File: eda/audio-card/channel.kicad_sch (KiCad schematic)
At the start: 2 parts, among them U3 74HCT541, U4 74HCT541

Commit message: Interim commit
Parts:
- removed U3, U4: 74HCT541, Package_DIP:DIP-20_W7.62mm, symbol 74xx:74HCT541
- added U1: 74LS74, symbol 74ls593:74LS74
- added U2, U5: 74LS593, Package_DIP:DIP-20_W7.62mm, symbol counters:74LS593
- added U4, U6: 74HCT574, Package_DIP:DIP-20_W7.62mm, symbol 74ls593:74HCT574
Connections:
- net D0: now also U5.1 (A), U6.2 (D0)
- net D1: now also U5.2 (B), U6.3 (D1)
- net D2: now also U5.3 (C), U6.4 (D2)
- net D3: now also U5.4 (D), U6.5 (D3)
- net D4: now also U5.5 (E), U6.6 (D4)
- net D5: now also U5.7 (G), U6.7 (D5)
- net D6: now also U5.7 (G), U6.8 (D6)
- net D7: now also U5.8 (H), U6.9 (D7)
- net GND: now also U2.10 (GND), U2.14 (~{CCKEN}), U4.10 (GND), U5.10 (GND), U6.1 (OE), U6.10 (GND)
- net VCC: now also U2.16 (RCK), U2.20 (VCC), U4.20 (VCC), U5.13 (CCK), U5.15 (CCKEN), U5.16 (RCK), U5.20 (VCC), U6.20 (VCC)
- new net: U2.1 (A), U6.19 (Q0)
- new net: U2.11 (~{RCO}), U5.14 (~{CCKEN})
- new net: U2.2 (B), U6.18 (Q1)
- new net: U2.3 (C), U6.17 (Q2)
- new net: U2.4 (D), U6.16 (Q3)
- new net: U2.5 (E), U6.15 (Q4)
- new net: U2.7 (G), U6.13 (Q6)
- new net: U2.7 (G), U6.14 (Q5)
- new net: U2.8 (H), U6.12 (Q7)
- new net: U1.3 (C), U5.11 (~{RCO})
- new net: U1.2 (D), U1.6 (~{Q})
- new net MainClock: U2.13 (CCK)
- new net Tone: U1.5 (Q), U4.1 (OE)
- new net ~{NoteLatch}: U2.17 (~{RCKEN}), U5.17 (~{RCKEN})
- new net ~{OctaveLatch}: U6.11 (Cp)
- new net ~{Reset}: U2.12 (~{CCLR}), U2.9 (~{CLOAD}), U5.12 (~{CCLR}), U5.9 (~{CLOAD})
- new net ~{VolumeLatch}: U4.11 (Cp)

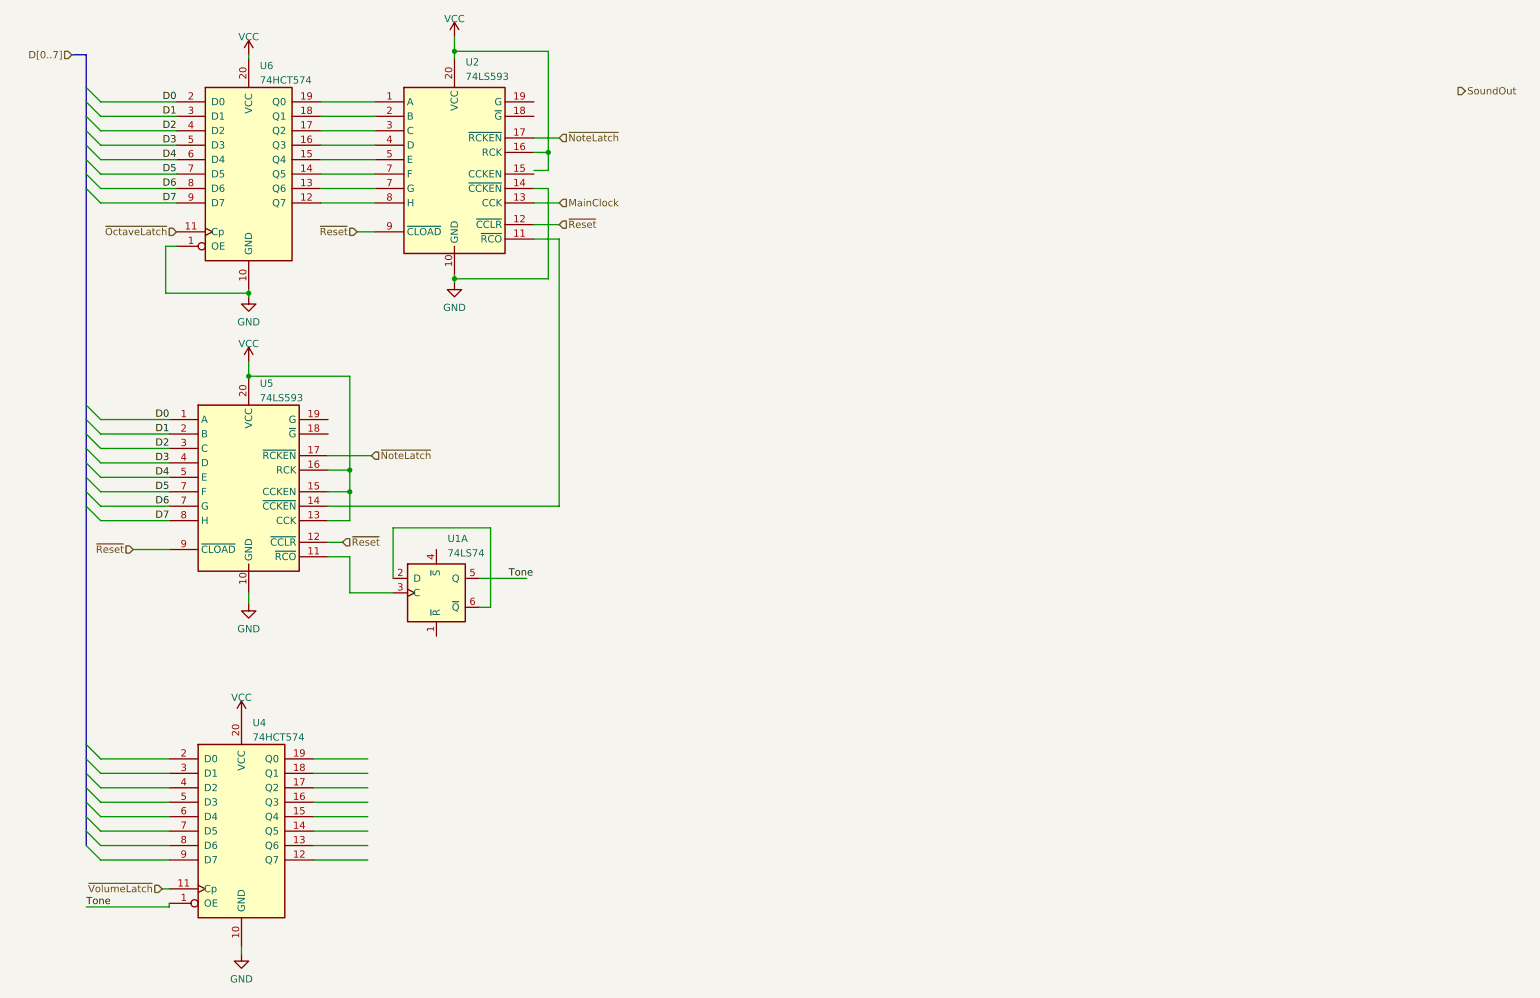
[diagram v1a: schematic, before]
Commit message: Start converting audio card to analog synth base
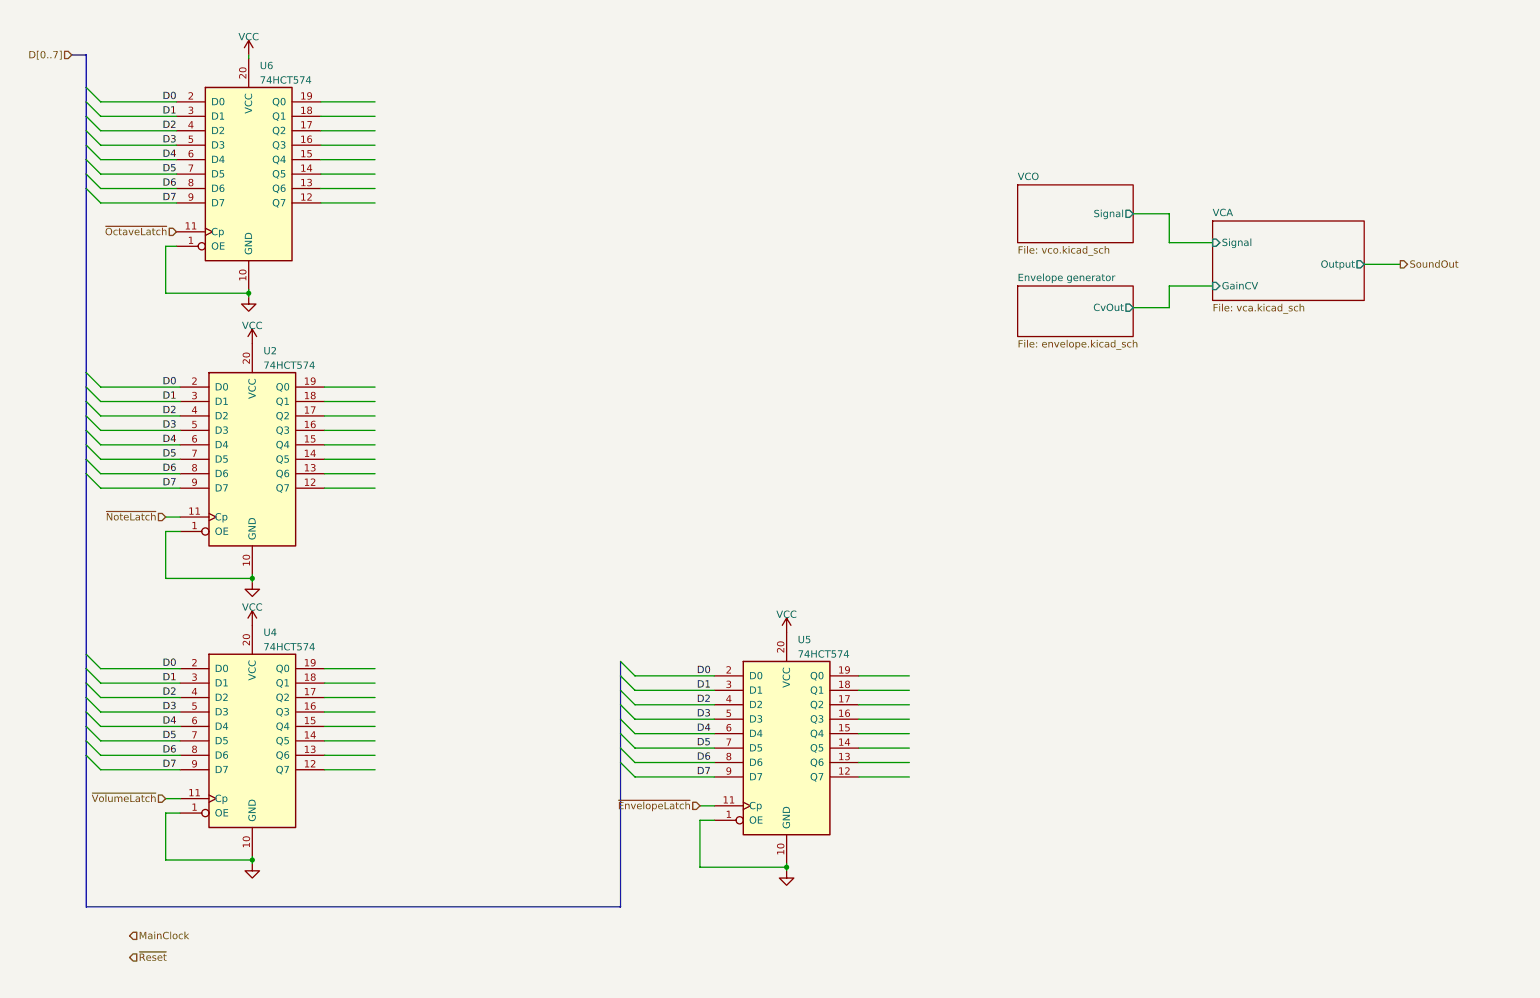
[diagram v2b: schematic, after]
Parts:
- removed U1: 74LS74, symbol 74ls593:74LS74
- removed U2, U5: 74LS593, Package_DIP:DIP-20_W7.62mm, symbol counters:74LS593
- added U2, U5: 74HCT574, Package_DIP:DIP-20_W7.62mm, symbol 74ls593:74HCT574
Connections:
- net Tone is gone; now on net GND: U4.1 (OE)
- net D0: now also U4.2 (D0), U2.2 (D0), U5.2 (D0)
- net D1: now also U4.3 (D1), U2.3 (D1), U5.3 (D1)
- net D2: now also U4.4 (D2), U2.4 (D2), U5.4 (D2)
- net D3: now also U4.5 (D3), U2.5 (D3), U5.5 (D3)
- net D4: now also U4.6 (D4), U2.6 (D4), U5.6 (D4)
- net D5: now also U4.7 (D5), U2.7 (D5), U5.7 (D5)
- net D6: now also U4.8 (D6), U2.8 (D6), U5.8 (D6)
- net D7: now also U4.9 (D7), U2.9 (D7), U5.9 (D7)
- net GND: now also U2.1 (OE), U2.10 (GND), U5.1 (OE), U5.10 (GND)
- net VCC: now also U2.20 (VCC), U5.20 (VCC)
- net ~{NoteLatch}: now also U2.11 (Cp)
- new net ~{EnvelopeLatch}: U5.11 (Cp)
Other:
- added sheet Envelope generator (envelope.kicad_sch)
- added sheet VCA (vca.kicad_sch)
- added sheet VCO (vco.kicad_sch)
